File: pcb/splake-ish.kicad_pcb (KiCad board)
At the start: 2 copper layers, 155.2 x 108.1 mm, 73 parts

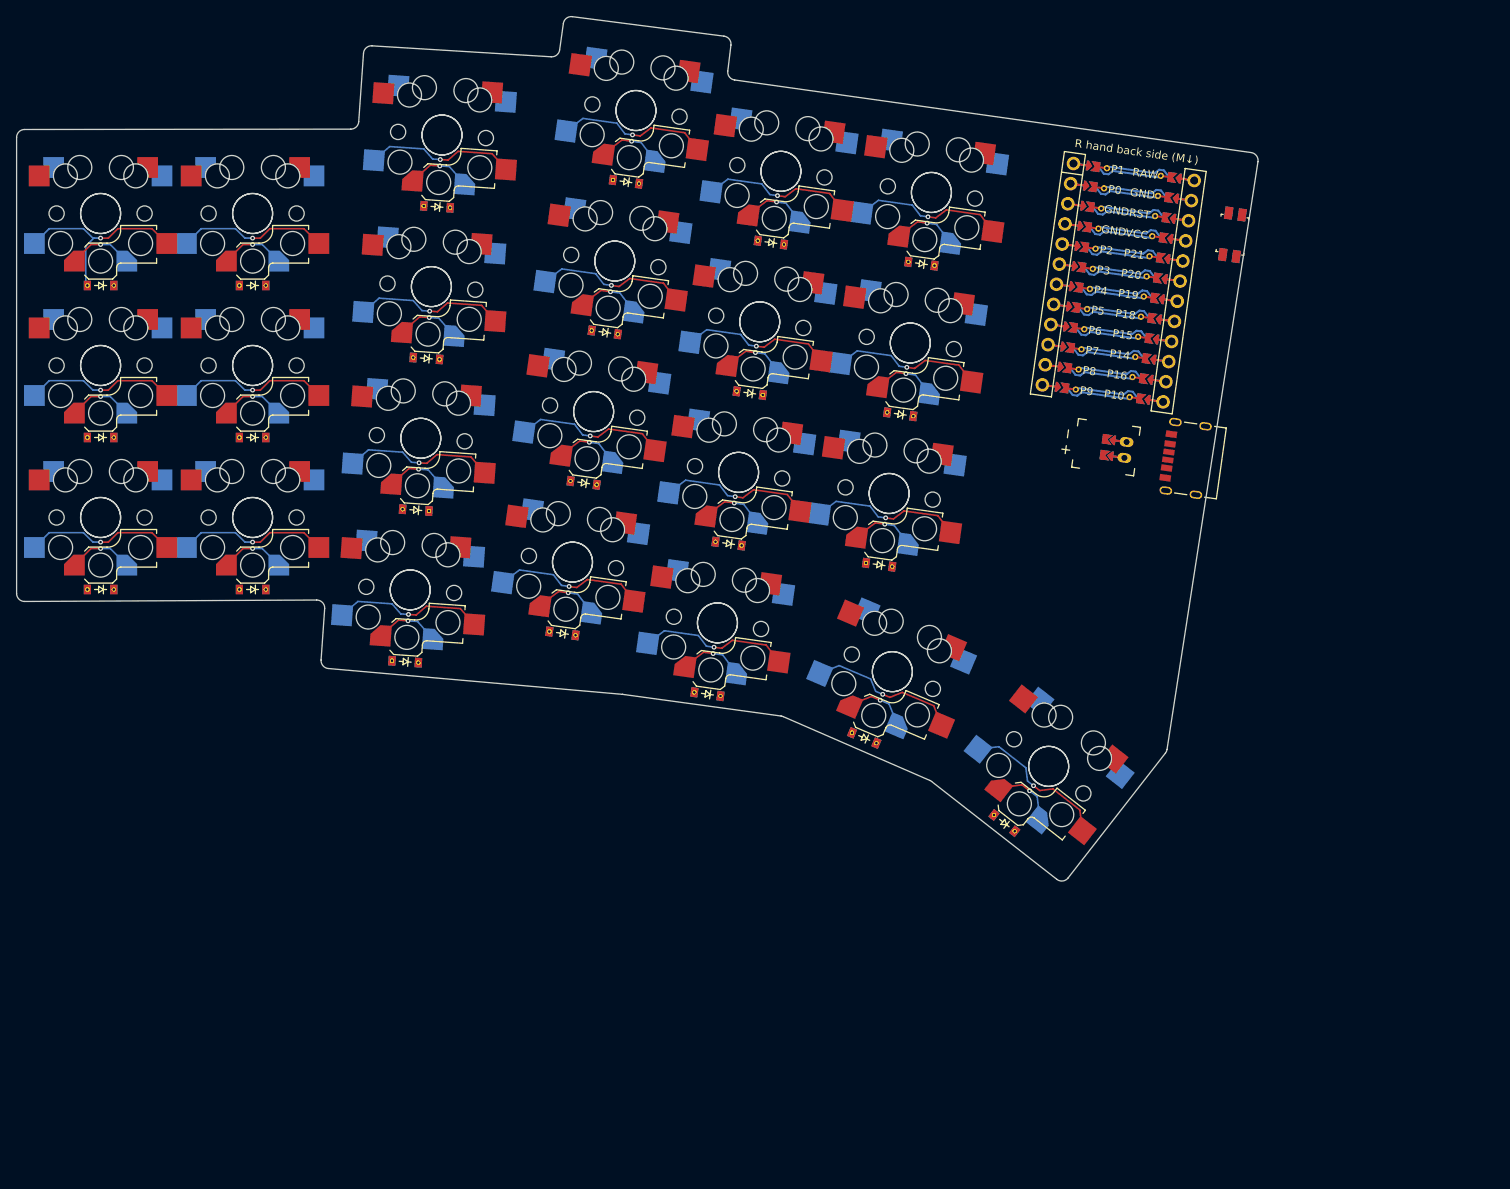
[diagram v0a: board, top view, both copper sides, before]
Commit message: updated pcbs and ergogen
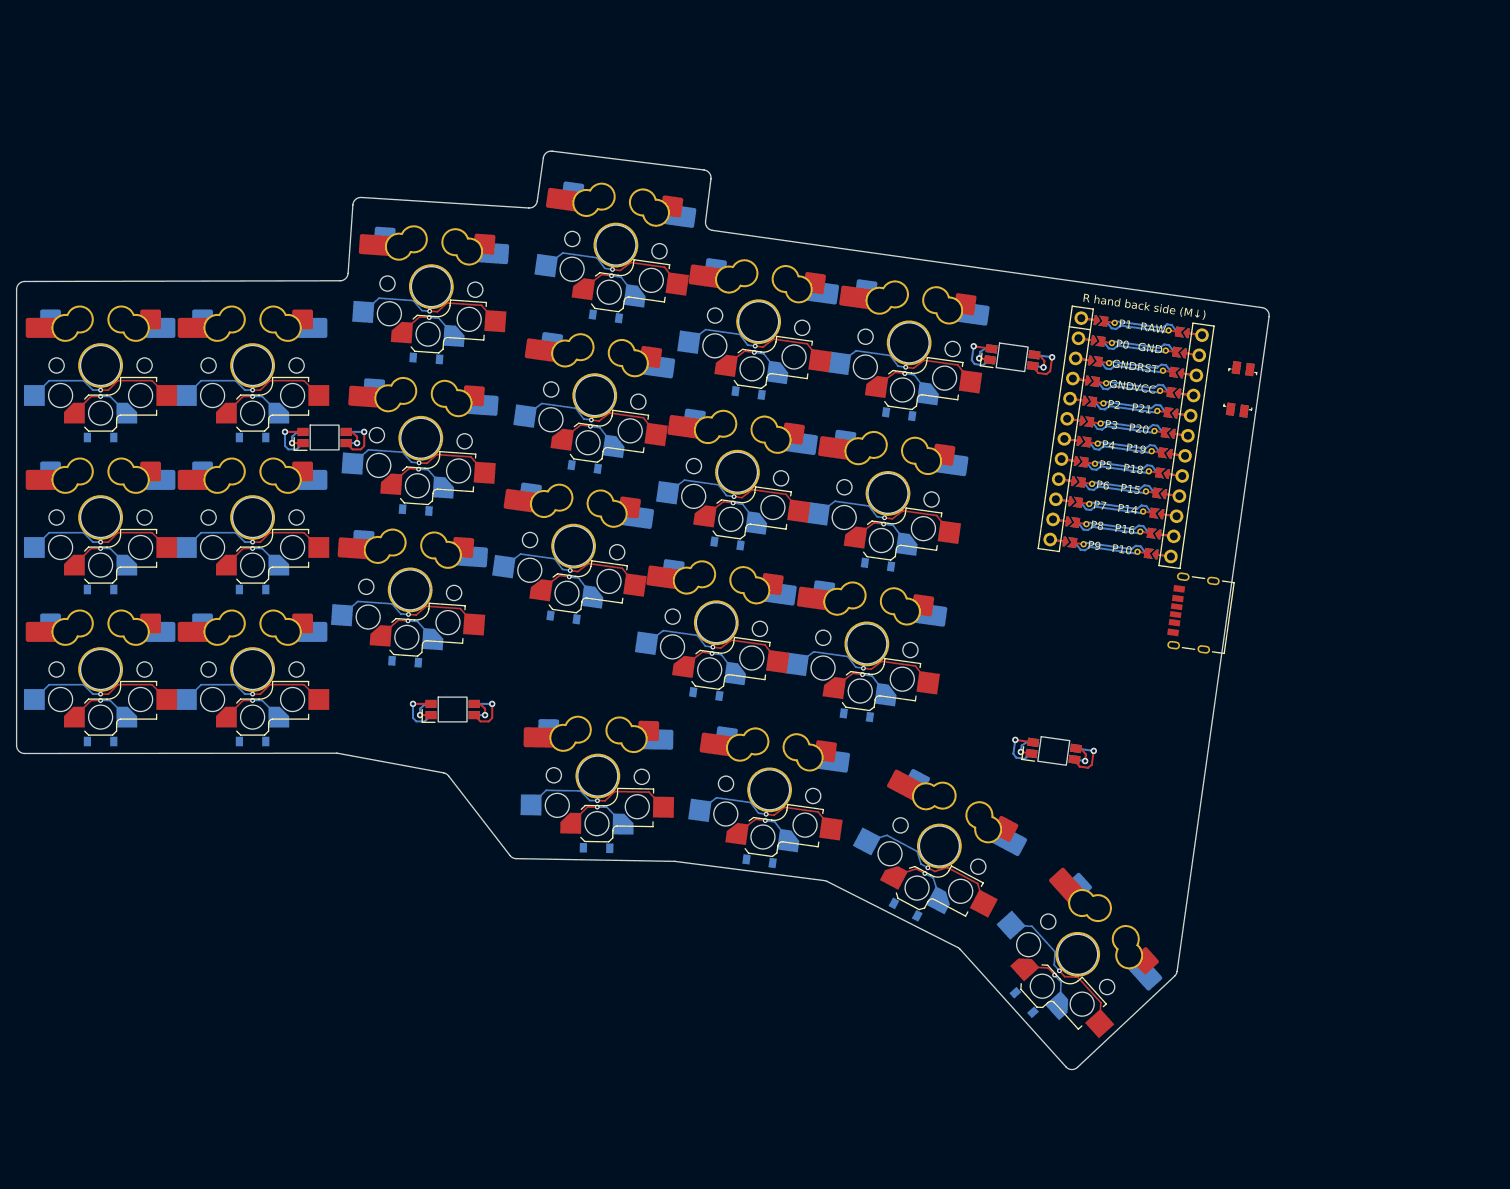
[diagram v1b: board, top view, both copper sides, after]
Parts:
- removed D23: , ComboDiode
- removed JST1: , ceoloide:battery_connector_jst_ph_2
- removed REF**: CUI_UJC-HP2-3-SMT-TR, CUI_UJC-HP2-3-SMT-TR
- removed XX10, XX11, XX12, XX13, XX14, XX15, XX16, XX17, XX18, XX19, XX2, XX20, XX21, XX22, XX23, XX3, XX4, XX5, XX6, XX7, XX8, XX9: , gateron-ks27-hotswap-reversible
- added LED1: , ceoloide:led_SK6812mini-e (per-key, reversible), B.Cu at (128.0, 91.0)
- added LED2: , ceoloide:led_SK6812mini-e (per-key, reversible), B.Cu at (144.0, 125.0)
- added LED3: , ceoloide:led_SK6812mini-e (per-key, reversible), B.Cu at (213.9, 81.0)
- added LED4: , ceoloide:led_SK6812mini-e (per-key, reversible), B.Cu at (219.1, 130.2)
- added S24: , ceoloide:switch_gateron_ks27_ks33, B.Cu at (100.0, 101.0)
- added S25: , ceoloide:switch_gateron_ks27_ks33, B.Cu at (100.0, 82.0)
- added S26: , ceoloide:switch_gateron_ks27_ks33, B.Cu at (119.0, 120.0)
- added S27: , ceoloide:switch_gateron_ks27_ks33, B.Cu at (119.0, 101.0)
- added S28: , ceoloide:switch_gateron_ks27_ks33, B.Cu at (119.0, 82.0)
- added S29: , ceoloide:switch_gateron_ks27_ks33, B.Cu at (138.7, 110.0)
- added S30: , ceoloide:switch_gateron_ks27_ks33, B.Cu at (140.0, 91.1)
- added S31: , ceoloide:switch_gateron_ks27_ks33, B.Cu at (141.3, 72.1)
- added S32: , ceoloide:switch_gateron_ks27_ks33, B.Cu at (159.1, 104.6)
- added S33: , ceoloide:switch_gateron_ks27_ks33, B.Cu at (161.8, 85.8)
- added S34: , ceoloide:switch_gateron_ks27_ks33, B.Cu at (164.4, 66.9)
- added S35: , ceoloide:switch_gateron_ks27_ks33, B.Cu at (177.0, 114.2)
- added S36: , ceoloide:switch_gateron_ks27_ks33, B.Cu at (179.6, 95.3)
- added S37: , ceoloide:switch_gateron_ks27_ks33, B.Cu at (182.3, 76.5)
- added S38: , ceoloide:switch_gateron_ks27_ks33, B.Cu at (195.8, 116.8)
- added S39: , ceoloide:switch_gateron_ks27_ks33, B.Cu at (198.4, 98.0)
- added S40: , ceoloide:switch_gateron_ks27_ks33, B.Cu at (201.1, 79.2)
- added S41: , ceoloide:switch_gateron_ks27_ks33, B.Cu at (183.6, 135.0)
- added S42: , ceoloide:switch_gateron_ks27_ks33, B.Cu at (204.9, 142.1)
- added S43: , ceoloide:switch_gateron_ks27_ks33, B.Cu at (222.1, 155.6)
- added S44: , ceoloide:switch_gateron_ks27_ks33, B.Cu at (162.2, 133.3)
- D1, D10, D11, D12, D13, D14, D15, D16, D17, D18, D19, D2, D20, D21, D22, D3, D4, D5, D6, D7, D8, D9: footprint ComboDiode -> ceoloide:diode_tht_sod123; moved to B.Cu
- S23: footprint ceoloide:switch_choc_v1_v2 -> ceoloide:switch_gateron_ks27_ks33
- XX1: footprint gateron-ks27-hotswap-reversible -> CUI_UJC-HP2-3-SMT-TR
- moved XX1 139.0 mm to (238.5, 113.2), turned to 82 degrees
- moved S23 119.1 mm to (100.0, 120.0), turned to 180 degrees
- moved S20 81.7 mm to (204.9, 142.1), turned to 152 degrees
- moved D20 80.8 mm to (200.6, 150.0), turned to 152 degrees
- moved S21 61.2 mm to (222.1, 155.6), turned to 132 degrees
- moved D19 58.6 mm to (182.4, 144.0)
- moved S19 58.6 mm to (183.6, 135.0)
- moved D21 55.3 mm to (215.4, 161.6), turned to 132 degrees
- moved S10 54.0 mm to (159.1, 104.6), turned to 172 degrees
- moved D10 53.7 mm to (157.9, 113.5), turned to 172 degrees
- moved S13 47.0 mm to (177.0, 114.2)
- moved S14 47.0 mm to (179.6, 95.3)
- moved D13 47.0 mm to (175.7, 123.1)
- moved D14 47.0 mm to (178.4, 104.3)
- moved S17 42.4 mm to (198.4, 98.0)
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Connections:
- D1 pad 1: outer-pinky_r1 -> P9
- D10 pad 1: ring_r3 -> P9
- D10 pad 2: ring_r3 -> middle_r1
- D11 pad 1: middle_r0 -> P10
- D11 pad 2: middle_r0 -> middle_r2
- D12 pad 1: middle_r1 -> P14
- D12 pad 2: middle_r1 -> middle_r3
- D13 pad 1: middle_r2 -> P9
- D13 pad 2: middle_r2 -> index_r1
- D14 pad 1: middle_r3 -> P10
- D14 pad 2: middle_r3 -> index_r2
- D15 pad 1: index_r1 -> P14
- D15 pad 2: index_r1 -> index_r3
- D16 pad 1: index_r2 -> P9
- D16 pad 2: index_r2 -> inner_r1
- D17 pad 1: index_r3 -> P10
- D17 pad 2: index_r3 -> inner_r2
- D18 pad 1: inner_r1 -> P14
- D18 pad 2: inner_r1 -> inner_r3
- D19 pad 1: inner_r2 -> P16
- D19 pad 2: inner_r2 -> 1_r1
- D2 pad 1: outer-pinky_r2 -> P10
- D20 pad 1: inner_r3 -> P16
- D20 pad 2: inner_r3 -> 2_r1
- D21 pad 1: 1_r0 -> P16
- D21 pad 2: 1_r0 -> 3_r1
- D22 pad 1: 2_r0 -> P16
- D22 pad 2: 2_r0 -> 1_r1
- D3 pad 1: outer-pinky_r3 -> P14
- D4 pad 1: pinky_r1 -> P9
- D5 pad 1: pinky_r2 -> P10
- D6 pad 1: pinky_r3 -> P14
- D7 pad 1: ring_r0 -> P9
- D7 pad 2: ring_r0 -> ring_r1
- D8 pad 1: ring_r1 -> P10
- D8 pad 2: ring_r1 -> ring_r2
- D9 pad 1: ring_r2 -> P14
- D9 pad 2: ring_r2 -> ring_r3
- S10 pad 1: P4 -> P5
- S10 pad 2: ring_r3 -> middle_r1
- S11 pad 2: middle_r0 -> middle_r2
- S12 pad 2: middle_r1 -> middle_r3
- S13 pad 1: P5 -> P6
- S13 pad 2: middle_r2 -> index_r1
- S14 pad 1: P5 -> P6
- S14 pad 2: middle_r3 -> index_r2
- S15 pad 2: index_r1 -> index_r3
- S16 pad 1: P6 -> P7
- S16 pad 2: index_r2 -> inner_r1
- S17 pad 1: P6 -> P7
- S17 pad 2: index_r3 -> inner_r2
- S18 pad 2: inner_r1 -> inner_r3
- S19 pad 1: P7 -> P5
- S19 pad 2: inner_r2 -> 1_r1
- S20 pad 1: P7 -> P6
- S20 pad 2: inner_r3 -> 2_r1
- S21 pad 1: P5 -> P7
- S21 pad 2: 1_r0 -> 3_r1
- S22 pad 1: P6 -> P4
- S22 pad 2: 2_r0 -> 1_r1
- S23 pad : (no net) -> outer-pinky_r1
- S23 pad 1: P7 -> P2
- S23 pad 2: 3_r0 -> outer-pinky_r1
- S7 pad 2: ring_r0 -> ring_r1
- S8 pad 2: ring_r1 -> ring_r2
- S9 pad 2: ring_r2 -> ring_r3
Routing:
- net (no net): track 0.00 -> 337.7 mm
- net rgb: track 0.00 -> 54.1 mm, vias 0 -> 8
- net 1_r1: track 0.00 -> 38.1 mm, vias 0 -> 2
- net 1_r0: track 19.1 -> 0.00 mm, vias 1 -> 0
- net 2_r0: track 19.1 -> 0.00 mm, vias 1 -> 0
- net 3_r0: track 19.1 -> 0.00 mm, vias 1 -> 0
- net 2_r1: track 0.00 -> 19.1 mm, vias 0 -> 1
- net 3_r1: track 0.00 -> 19.1 mm, vias 0 -> 1
- net middle_r0: track 19.1 -> 0.00 mm, vias 1 -> 0
- net ring_r0: track 19.1 -> 0.00 mm, vias 1 -> 0
- net P5: track 51.2 -> 33.1 mm, vias 5 -> 4
- net GND: track 29.5 -> 15.0 mm, vias 0 -> 4
- net P6: track 42.9 -> 33.1 mm
- net P7: track 42.9 -> 33.1 mm
- net P2: track 34.6 -> 24.8 mm
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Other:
- board size 155.2 x 108.1 mm -> 156.6 x 114.8 mm

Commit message: updated footprints
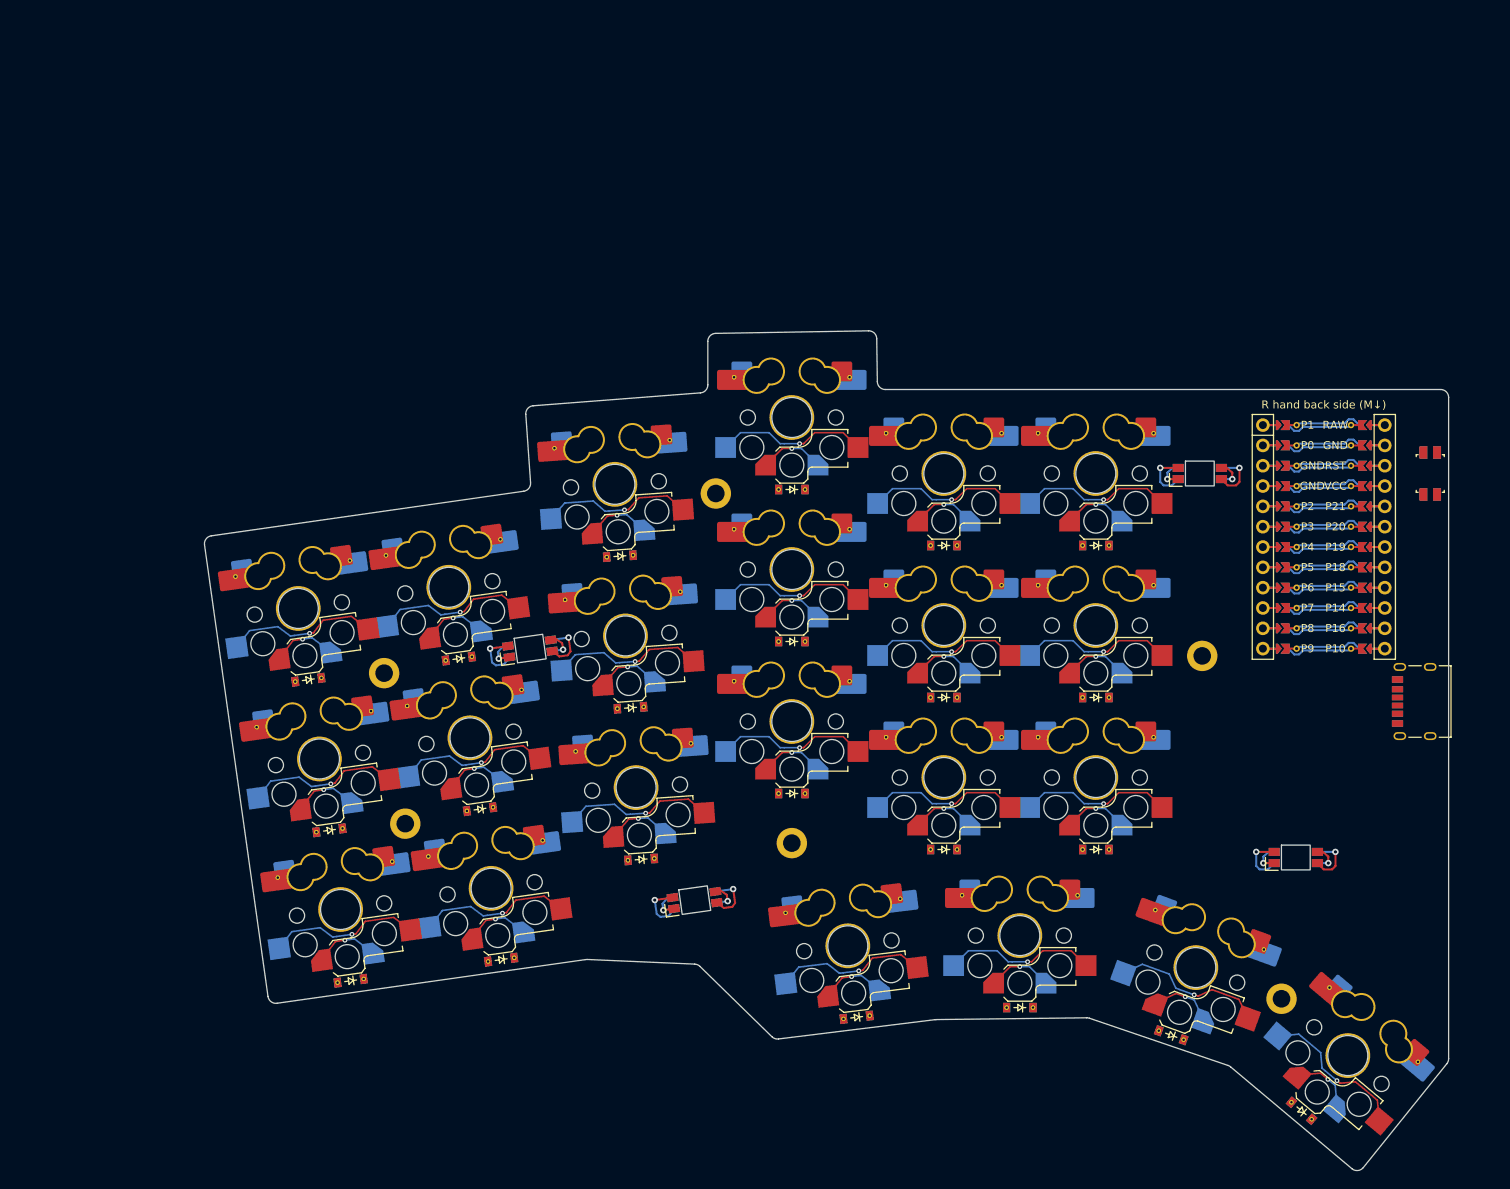
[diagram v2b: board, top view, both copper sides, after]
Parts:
- added H1: , ceoloide:mounting_hole_plated, F.Cu at (135.4, 120.5)
- added H2: , ceoloide:mounting_hole_plated, F.Cu at (138.1, 139.3)
- added H3: , ceoloide:mounting_hole_plated, F.Cu at (176.9, 98.0)
- added H4: , ceoloide:mounting_hole_plated, F.Cu at (186.4, 141.7)
- added H5: , ceoloide:mounting_hole_plated, F.Cu at (237.7, 118.3)
- added H6: , ceoloide:mounting_hole_plated, F.Cu at (247.6, 161.2)
- added REF**: VIA-0.6mm, VIA-0.6mm, F.Cu at (122.1, 146.0)
- added REF**: VIA-0.6mm, VIA-0.6mm, F.Cu at (179.2, 121.5)
- added REF**: VIA-0.6mm, VIA-0.6mm, F.Cu at (179.2, 102.5)
- added REF**: VIA-0.6mm, VIA-0.6mm, F.Cu at (179.2, 83.5)
- added REF**: VIA-0.6mm, VIA-0.6mm, F.Cu at (198.2, 128.5)
- added REF**: VIA-0.6mm, VIA-0.6mm, F.Cu at (198.2, 109.5)
- added REF**: VIA-0.6mm, VIA-0.6mm, F.Cu at (198.2, 90.5)
- added REF**: VIA-0.6mm, VIA-0.6mm, F.Cu at (217.2, 128.5)
- added REF**: VIA-0.6mm, VIA-0.6mm, F.Cu at (217.2, 109.5)
- added REF**: VIA-0.6mm, VIA-0.6mm, F.Cu at (217.2, 90.5)
- added REF**: VIA-0.6mm, VIA-0.6mm, F.Cu at (207.7, 148.2)
- added REF**: VIA-0.6mm, VIA-0.6mm, F.Cu at (119.5, 127.2)
- added REF**: VIA-0.6mm, VIA-0.6mm, F.Cu at (231.8, 150.1)
- added REF**: VIA-0.6mm, VIA-0.6mm, F.Cu at (253.6, 159.8)
- added REF**: VIA-0.6mm, VIA-0.6mm, F.Cu at (185.6, 150.4)
- added REF**: VIA-0.6mm, VIA-0.6mm, F.Cu at (136.4, 144.0)
- added REF**: VIA-0.6mm, VIA-0.6mm, F.Cu at (133.8, 125.2)
- added REF**: VIA-0.6mm, VIA-0.6mm, F.Cu at (131.2, 106.4)
- added REF**: VIA-0.6mm, VIA-0.6mm, F.Cu at (155.3, 141.4)
- added REF**: VIA-0.6mm, VIA-0.6mm, F.Cu at (152.6, 122.5)
- added REF**: VIA-0.6mm, VIA-0.6mm, F.Cu at (150.0, 103.7)
- added REF**: VIA-0.6mm, VIA-0.6mm, F.Cu at (173.8, 129.2)
- added REF**: VIA-0.6mm, VIA-0.6mm, F.Cu at (116.9, 108.4)
- added REF**: VIA-0.6mm, VIA-0.6mm, F.Cu at (172.5, 110.3)
- added REF**: VIA-0.6mm, VIA-0.6mm, F.Cu at (171.1, 91.3)
- added REF**: VIA-0.6mm, VIA-0.6mm, F.Cu at (193.6, 121.5)
- added REF**: VIA-0.6mm, VIA-0.6mm, F.Cu at (193.6, 102.5)
- added REF**: VIA-0.6mm, VIA-0.6mm, F.Cu at (193.6, 83.5)
- added REF**: VIA-0.6mm, VIA-0.6mm, F.Cu at (212.6, 128.5)
- added REF**: VIA-0.6mm, VIA-0.6mm, F.Cu at (212.6, 109.5)
- added REF**: VIA-0.6mm, VIA-0.6mm, F.Cu at (212.6, 90.5)
- added REF**: VIA-0.6mm, VIA-0.6mm, F.Cu at (231.6, 128.5)
- added REF**: VIA-0.6mm, VIA-0.6mm, F.Cu at (231.6, 109.5)
- added REF**: VIA-0.6mm, VIA-0.6mm, F.Cu at (141.0, 143.4)
- added REF**: VIA-0.6mm, VIA-0.6mm, F.Cu at (231.6, 90.5)
- added REF**: VIA-0.6mm, VIA-0.6mm, F.Cu at (222.1, 148.2)
- added REF**: VIA-0.6mm, VIA-0.6mm, F.Cu at (245.4, 155.0)
- added REF**: VIA-0.6mm, VIA-0.6mm, F.Cu at (264.7, 169.0)
- added REF**: VIA-0.6mm, VIA-0.6mm, F.Cu at (200.0, 148.7)
- added REF**: VIA-0.6mm, VIA-0.6mm, F.Cu at (138.3, 124.6)
- added REF**: VIA-0.6mm, VIA-0.6mm, F.Cu at (135.7, 105.7)
- added REF**: VIA-0.6mm, VIA-0.6mm, F.Cu at (159.4, 130.2)
- added REF**: VIA-0.6mm, VIA-0.6mm, F.Cu at (158.1, 111.3)
- added REF**: VIA-0.6mm, VIA-0.6mm, F.Cu at (156.7, 92.3)
- D1, D10, D11, D12, D13, D14, D15, D16, D17, D18, D19, D2, D20, D21, D22, D3, D4, D5, D6, D7, D8, D9: footprint ceoloide:diode_tht_sod123 -> ComboDiode; moved to F.Cu
- moved D1 43.3 mm to (131.3, 158.9), turned to 188 degrees
- moved S1 42.4 mm to (130.0, 150.0), turned to 188 degrees
- moved S23 42.4 mm to (130.0, 150.0), turned to 188 degrees
- moved D2 41.5 mm to (128.6, 140.1), turned to 188 degrees
- moved D4 41.3 mm to (150.1, 156.3), turned to 188 degrees
- moved S2 40.7 mm to (127.4, 131.2), turned to 188 degrees
- moved S24 40.7 mm to (127.4, 131.2), turned to 188 degrees
- moved S26 40.5 mm to (148.8, 147.4), turned to 188 degrees
- moved S4 40.5 mm to (148.8, 147.4), turned to 188 degrees
- moved D3 39.9 mm to (126.0, 121.3), turned to 188 degrees
- moved D5 39.5 mm to (147.4, 137.5), turned to 188 degrees
- moved S25 39.2 mm to (124.7, 112.4), turned to 188 degrees
- moved S3 39.2 mm to (124.7, 112.4), turned to 188 degrees
- moved D22 38.8 mm to (194.5, 163.5), turned to 187 degrees
- moved S27 38.7 mm to (146.2, 128.5), turned to 188 degrees
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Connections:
- D1 pad 1: P9 -> outer-pinky_r1
- D10 pad 1: P9 -> middle_r1
- D11 pad 1: P10 -> middle_r2
- D12 pad 1: P14 -> middle_r3
- D13 pad 1: P9 -> index_r1
- D14 pad 1: P10 -> index_r2
- D15 pad 1: P14 -> index_r3
- D16 pad 1: P9 -> inner_r1
- D17 pad 1: P10 -> inner_r2
- D18 pad 1: P14 -> inner_r3
- D19 pad 1: P16 -> 1_r1
- D2 pad 1: P10 -> outer-pinky_r2
- D20 pad 1: P16 -> 2_r1
- D21 pad 1: P16 -> 3_r1
- D22 pad 1: P16 -> 1_r1
- D3 pad 1: P14 -> outer-pinky_r3
- D4 pad 1: P9 -> pinky_r1
- D5 pad 1: P10 -> pinky_r2
- D6 pad 1: P14 -> pinky_r3
- D7 pad 1: P9 -> ring_r1
- D8 pad 1: P10 -> ring_r2
- D9 pad 1: P14 -> ring_r3
- RST1 pad 1: inner_r3 -> RST
- RST1 pad 3: inner_r3 -> RST
- XX1 pad A5: CC1 -> CC2
- XX1 pad B5: CC2 -> CC1
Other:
- board size 156.6 x 114.8 mm -> 155.5 x 105 mm
